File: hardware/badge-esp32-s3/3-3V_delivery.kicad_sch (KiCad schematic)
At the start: 5 parts, among them U2 NCP167BMX330TBG

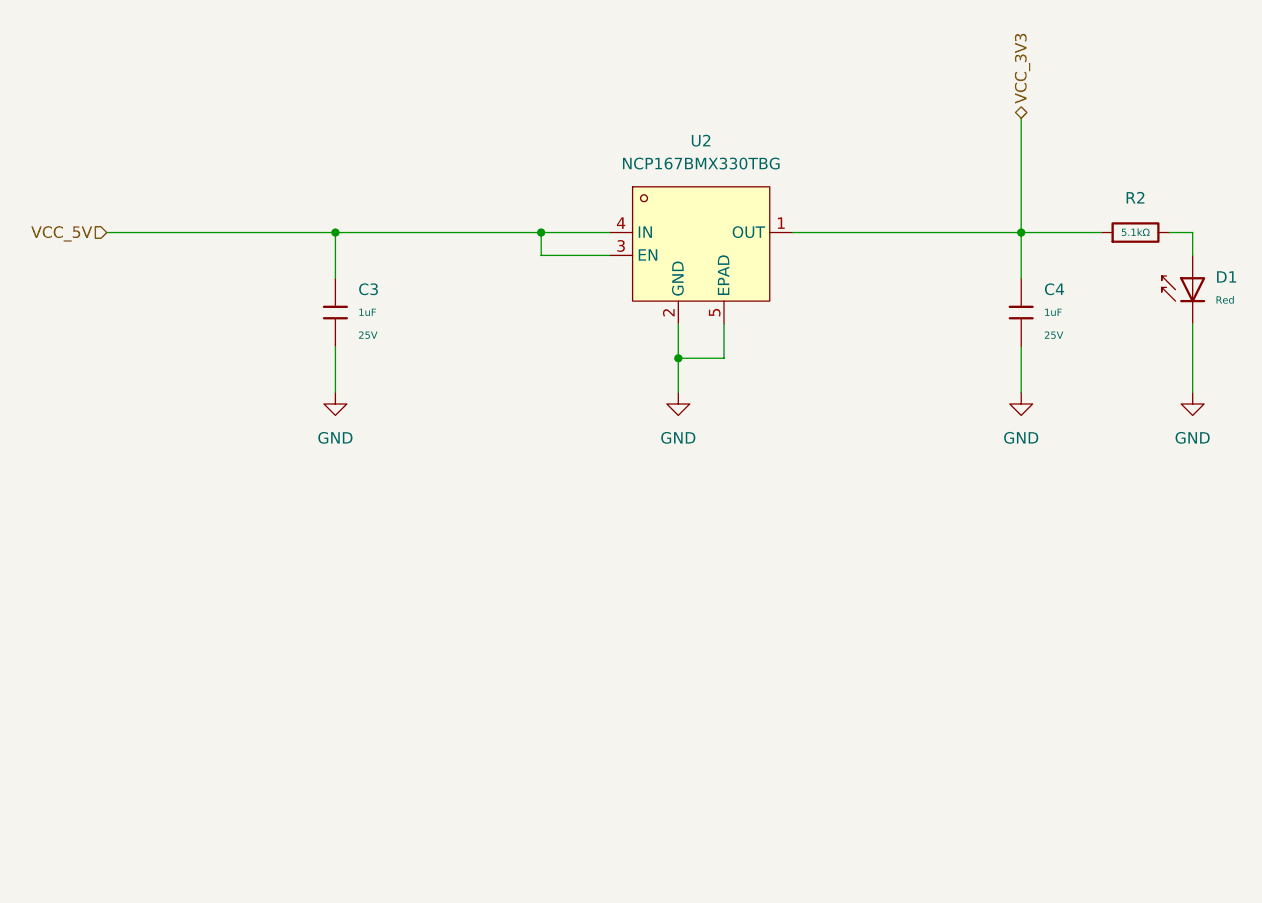
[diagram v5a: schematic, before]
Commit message: Started adding the circuitry for the 5V voltage booster.
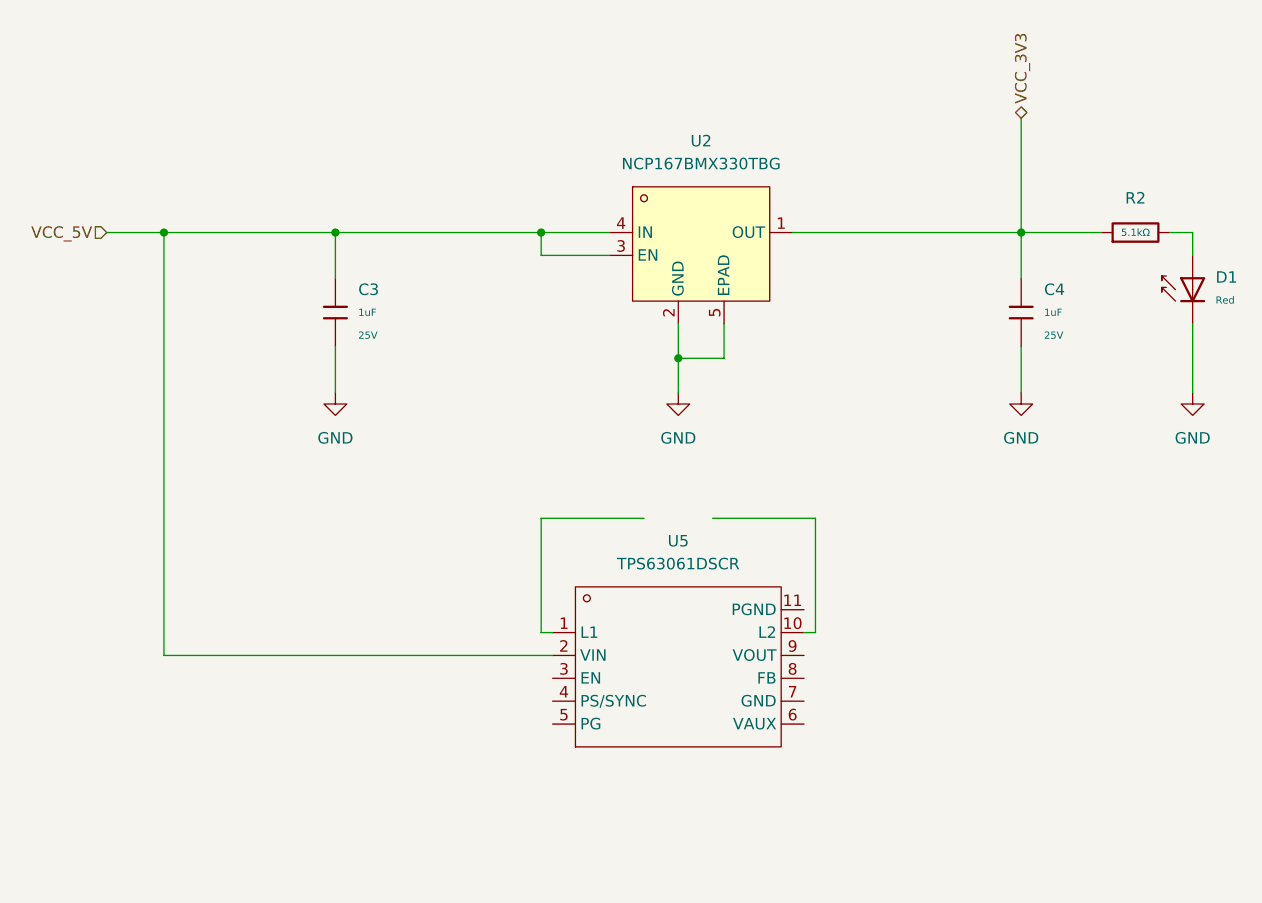
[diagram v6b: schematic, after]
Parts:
- added U5: TPS63061DSCR, lcsc-lib:WSON-10_L3.0-W3.0-P0.50-BL-EP-A, symbol lcsc-lib:TPS63061DSCR
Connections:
- net VCC_5V: now also U5.2 (VIN)
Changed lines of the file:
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@@
+	)
+	(junction
+		(at 88.9 63.5)
+		(diameter 0)
+		(color 0 0 0 0)
 	)
 	(junction
@@
 	(wire
 		(pts
+			(xy 88.9 63.5) (xy 107.95 63.5)
+		)
+		(stroke
+			(width 0)
+			(type default)
+		)
+	)
+	(wire
+		(pts
 			(xy 203.2 63.5) (xy 203.2 66.04)
 		)
@@
 	(wire
 		(pts
+			(xy 130.81 95.25) (xy 130.81 107.95)
+		)
+		(stroke
+			(width 0)
+			(type default)
+		)
+	)
+	(wire
+		(pts
 			(xy 184.15 63.5) (xy 184.15 68.58)
 		)
@@
 	(wire
 		(pts
-			(xy 82.55 63.5) (xy 107.95 63.5)
+			(xy 82.55 63.5) (xy 88.9 63.5)
 		)
 		(stroke
@@
 	(wire
 		(pts
+			(xy 161.29 107.95) (xy 161.29 95.25)
+		)
+		(stroke
+			(width 0)
+			(type default)
+		)
+	)
+	(wire
+		(pts
+			(xy 130.81 107.95) (xy 132.08 107.95)
+		)
+		(stroke
+			(width 0)
+			(type default)
+		)
+	)
+	(wire
+		(pts
 			(xy 146.05 77.47) (xy 146.05 81.28)
 		)
@@
 	(wire
 		(pts
+			(xy 160.02 107.95) (xy 161.29 107.95)
+		)
+		(stroke
+			(width 0)
+			(type default)
+		)
+	)
+	(wire
+		(pts
 			(xy 184.15 63.5) (xy 193.04 63.5)
 		)
@@
 	(wire
 		(pts
+			(xy 88.9 63.5) (xy 88.9 110.49)
+		)
+		(stroke
+			(width 0)
+			(type default)
+		)
+	)
+	(wire
+		(pts
 			(xy 130.81 66.04) (xy 138.43 66.04)
+		)
+		(stroke
+			(width 0)
+			(type default)
+		)
+	)
+	(wire
+		(pts
+			(xy 142.24 95.25) (xy 130.81 95.25)
+		)
+		(stroke
+			(width 0)
+			(type default)
+		)
+	)
+	(wire
+		(pts
+			(xy 88.9 110.49) (xy 132.08 110.49)
+		)
+		(stroke
+			(width 0)
+			(type default)
+		)
+	)
+	(wire
+		(pts
+			(xy 161.29 95.25) (xy 149.86 95.25)
 		)
 		(stroke
@@
 					(unit 1)
 				)
+			)
+		)
+	)
+	(symbol
+		(lib_id "lcsc-lib:TPS63061DSCR")
+		(at 146.05 111.76 0)
+		(unit 1)
+		(exclude_from_sim no)
+		(in_bom yes)
+		(on_board yes)
+		(dnp no)
+		(fields_autoplaced yes)
+		(property "Reference" "U5"
+			(at 146.05 97.79 0)
+			(effects
+				(font
+					(size 1.27 1.27)
+				)
+			)
+		)
+		(property "Value" "TPS63061DSCR"
+			(at 146.05 100.33 0)
+			(effects
+				(font
+					(size 1.27 1.27)
+				)
+			)
+		)
+		(property "Footprint" "lcsc-lib:WSON-10_L3.0-W3.0-P0.50-BL-EP-A"
+			(at 146.05 111.76 0)
+			(effects
+				(font
+					(size 1.27 1.27)
+				)
+				(hide yes)
+			)
+		)
+		(property "Datasheet" "https://www.ti.com/cn/lit/gpn/tps63060"
+			(at 146.05 111.76 0)
+			(effects
+				(font
+					(size 1.27 1.27)
+				)
+				(hide yes)
+			)
+		)
+		(property "Description" "Function:Boost type Output Type:Adjustable and Fixed Input Voltage:2.5V~12V Input Voltage:2.5V~12V Output Voltage:5V Output Voltage:5V Output Current:1.3A Switching Frequency:2.4MHz Switching Frequency:2.4MHz Operating Temperature:-40°C~+85°C@(TA) Operating"
+			(at 146.05 111.76 0)
+			(effects
+				(font
+					(size 1.27 1.27)
+				)
+				(hide yes)
+			)
+		)
+		(property "Manufacturer Part" "TPS63061DSCR"
+			(at 146.05 111.76 0)
+			(effects
+				(font
+					(size 1.27 1.27)
+				)
+				(hide yes)
+			)
+		)
+		(property "Manufacturer" "TI(德州仪器)"
+			(at 146.05 111.76 0)
+			(effects
+				(font
+					(size 1.27 1.27)
+				)
+				(hide yes)
+			)
+		)
+		(property "Supplier Part" "C2876326"
+			(at 146.05 111.76 0)
+			(effects
+				(font
+					(size 1.27 1.27)
+				)
+				(hide yes)
+			)
+		)
+		(property "Supplier" "LCSC"
+			(at 146.05 111.76 0)
+			(effects
+				(font
+					(size 1.27 1.27)
+				)
+				(hide yes)
+			)
+		)
+		(property "LCSC Part Name" "2A高输入电压降压-升压转换器"
+			(at 146.05 111.76 0)
+			(effects
+				(font
+					(size 1.27 1.27)
+				)
+				(hide yes)
+			)
+		)
+		(pin "1"
+		)
+		(pin "2"
+		)
+		(pin "3"
+		)
+		(pin "6"
+		)
+		(pin "7"
+		)
+		(pin "8"
+		)
+		(pin "4"
+		)
+		(pin "10"
+		)
+		(pin "9"
+		)
+		(pin "11"
+		)
+		(pin "5"
+		)
+		(instances
+			(project ""
+				(path "/e2af9a6c-dbe9-4de2-9ba6-ea213a7300ec/f36e3e2c-eb39-474f-a489-171fecc16703"
+					(reference "U5")
+					(unit 1)
+				)

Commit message: Added capacitors and inductors for the buck boost converter.
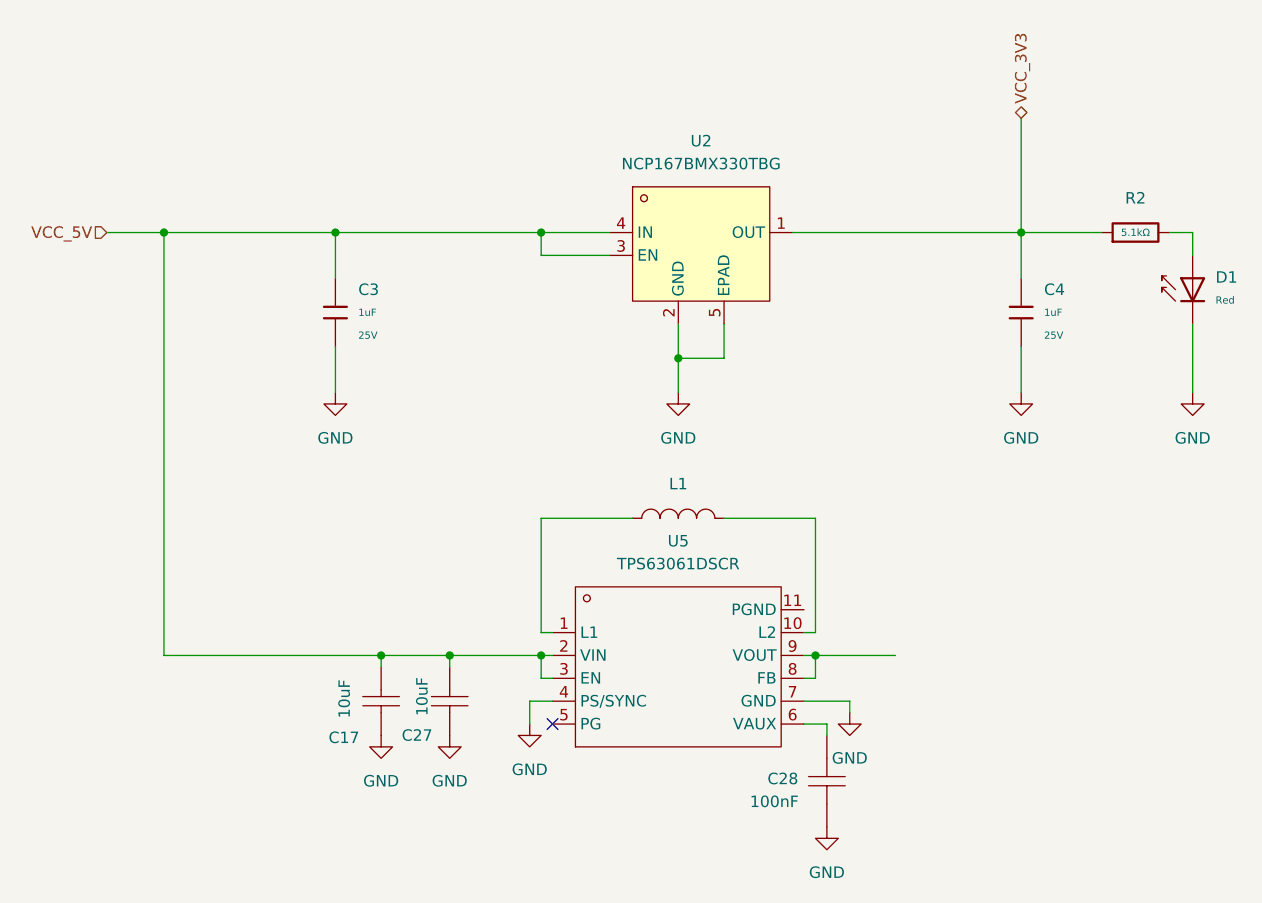
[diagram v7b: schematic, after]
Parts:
- added C17, C27: 10uF, lcsc-lib:C0805, symbol lcsc-lib:EMK212BJ106KG-T
- added C28: 100nF, lcsc-lib:C0201, symbol lcsc-lib:CL03A104KP3NNNC
- added L1: 1uH, 1uH_inductor:IND-SMD_L4.0-W4.0_XFL4020-102MEB, symbol lcsc-lib:XFL4020-102MEC
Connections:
- net GND: now also U5.4 (PS/SYNC), U5.7 (GND), C17.1, C27.1, C28.1
- net VCC_5V: now also U5.3 (EN), C17.2, C27.2
- net at U5.1 (L1): now also L1.1
- net at U5.10 (L2): now also L1.2
- net at U5.6 (VAUX): now also C28.2
- net at U5.8 (FB): now also U5.9 (VOUT)
- no-connect marks 0 -> 1

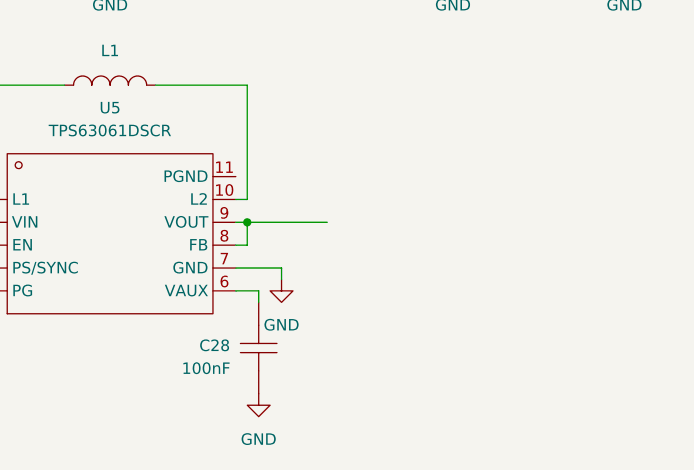
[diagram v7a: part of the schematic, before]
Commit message: Added capacitors for the 5V booster circuit.
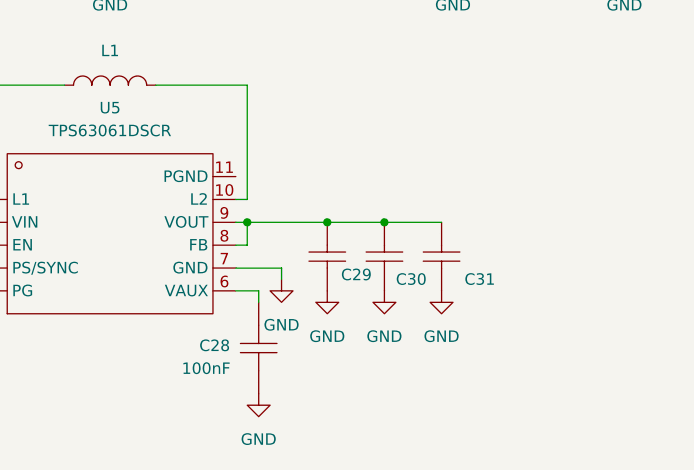
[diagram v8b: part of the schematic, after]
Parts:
- added C29, C30, C31: 22uF, lcsc-lib:C0805, symbol lcsc-lib:EMK212BBJ226MG-T
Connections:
- net GND: now also C29.1, C30.1, C31.1
- net at U5.8 (FB), U5.9 (VOUT): now also C29.2, C30.2, C31.2
